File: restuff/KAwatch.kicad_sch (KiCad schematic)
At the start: 15 parts, among them J1 Conn_01x08, J2 USB_C_Receptacle_PowerOnly_6P, J3 Conn_01x02, J4 Conn_01x02, Q1 Q_NPN_BCE, SW1 SW_Push, U1 ESP32-WROOM-32E, U2 MCP73831-2-OT, U3 AMS1117-3.3

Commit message: testing bullshi
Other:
- note added: "Nig"
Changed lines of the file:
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@@
+		)
+	)
+	(text "Nig"
+		(exclude_from_sim no)
+		(at 209.804 127.508 0)
+		(effects
+			(font
+				(size 1.27 1.27)
+			)
 		)
 	)

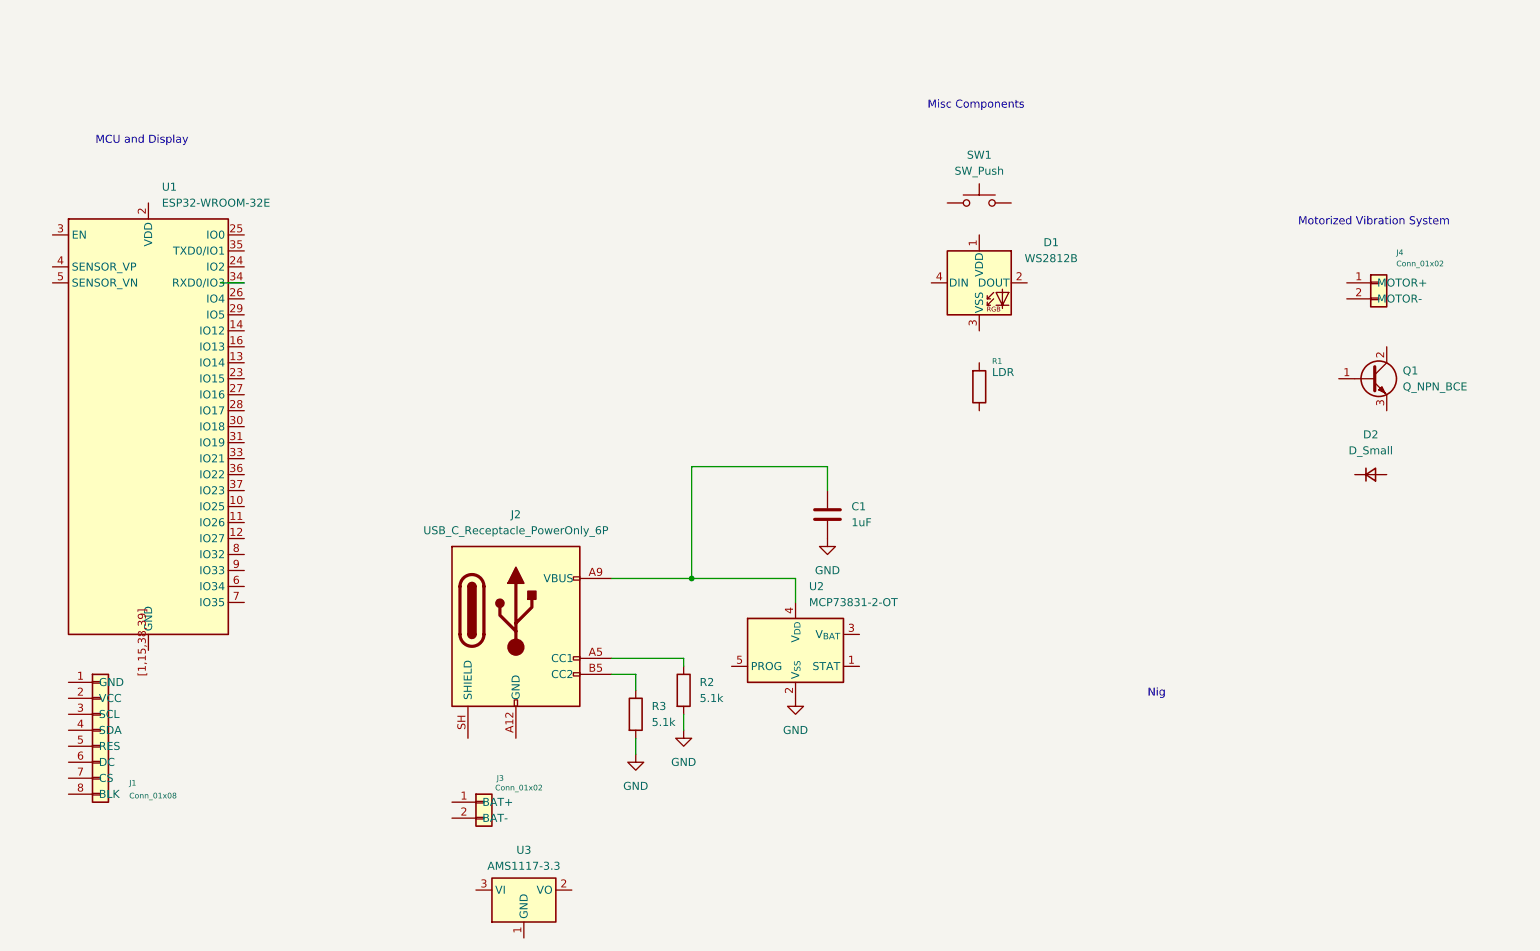
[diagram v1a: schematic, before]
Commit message: added more wires to powerchain
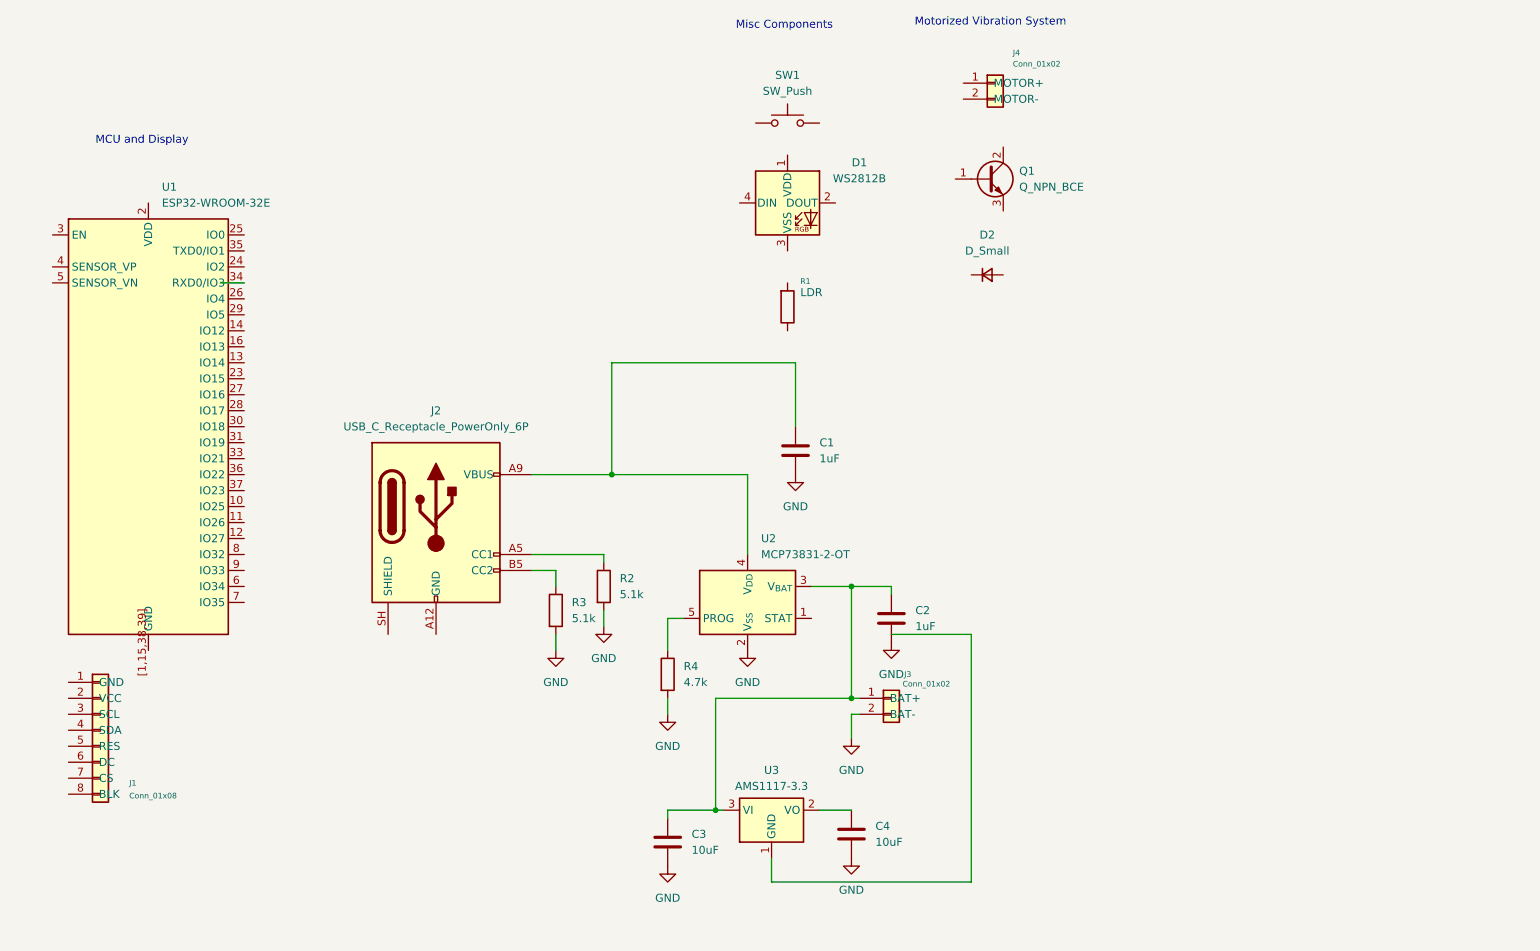
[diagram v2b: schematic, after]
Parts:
- added C2: 1uF, symbol Device:C
- added C3, C4: 10uF, symbol Device:C
- added R4: 4.7k, symbol Device:R
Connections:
- net GND: now also J3.2 (BAT-), C2.2, C3.2, C4.2, R4.2
- net at U2.3 (V_{BAT}): now also J3.1 (BAT+), U3.3 (VI), C2.1, C3.1
- net at U2.5 (PROG): now also R4.1
- net at U3.2 (VO): now also C4.1
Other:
- note removed: "Nig"
- moved on the sheet: C1, D1, D2, J2, J3, J4, Q1, R1, R2, R3, SW1, U2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

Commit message: connections to display
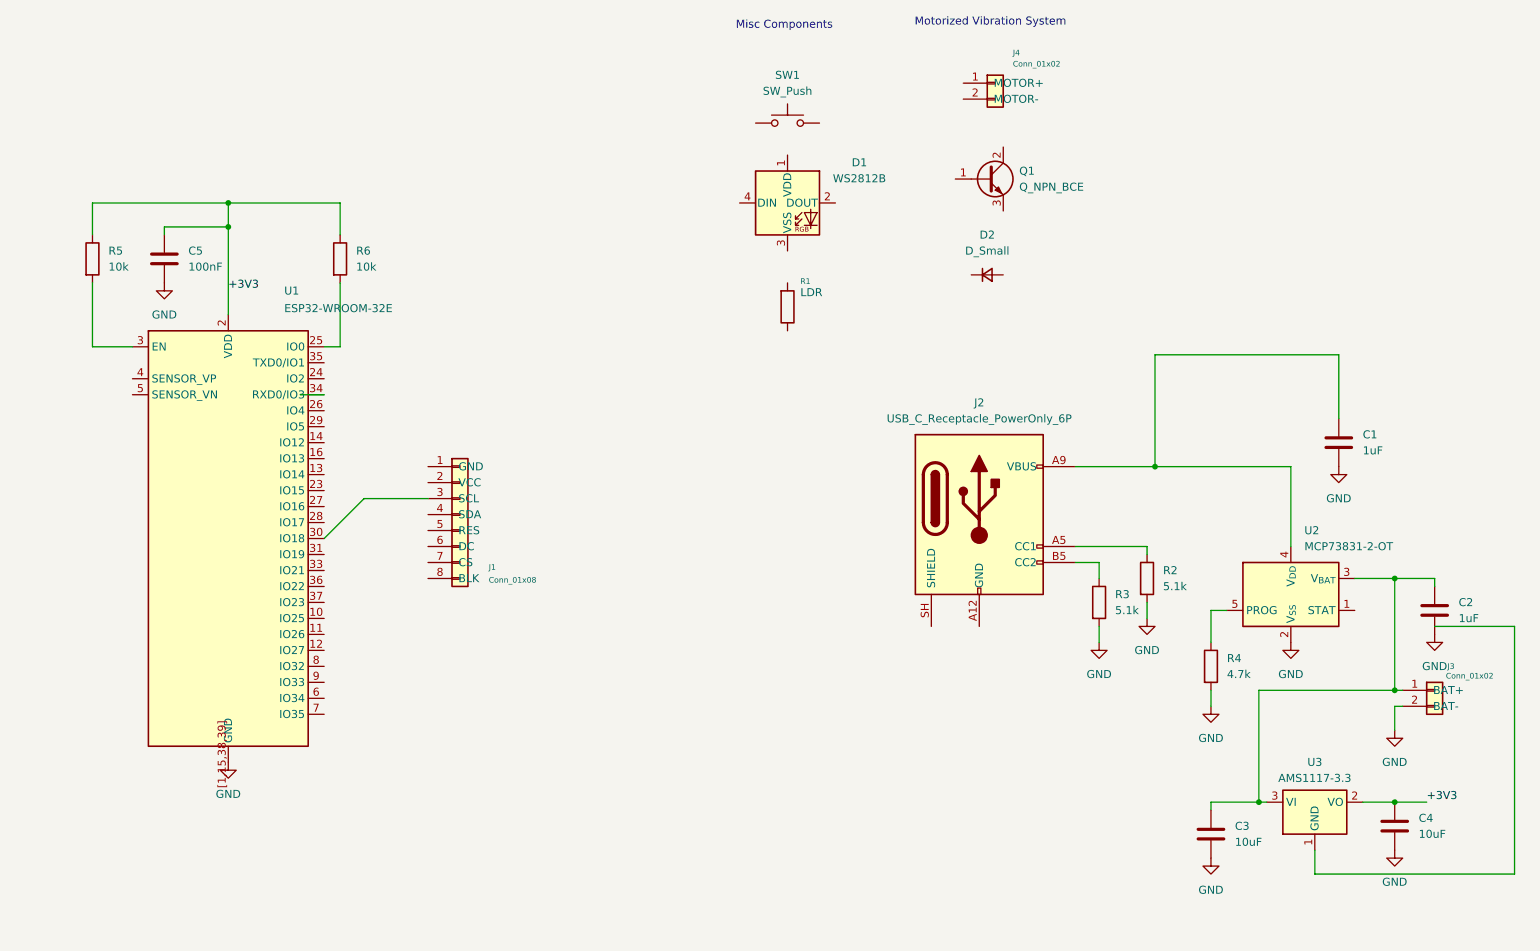
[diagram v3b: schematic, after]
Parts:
- added C5: 100nF, symbol Device:C
- added R5, R6: 10k, symbol Device:R
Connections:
- net GND: now also U1.[1,15,38,39] (GND), C5.2
- net at J1.3 (SCL): now also U1.30 (IO18)
- net +3V3: now reaches C4.1, U3.2 (VO)
- net +3V3: now also U1.2 (VDD), C5.1, R5.1, R6.1
- net at U1.25 (IO0): now also R6.2
- net at U1.3 (EN): now also R5.2
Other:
- note removed: "MCU and Display"
- moved on the sheet: C1, C2, C3, C4, J1, J2, J3, R2, R3, R4, U1, U2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

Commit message: display connector done
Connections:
- net at J1.3 (SCL), U1.30 (IO18): no longer names the net of J1.3 (SCL), U1.30 (IO18)
- net DISP_MOSI: now reaches J1.4 (SDA)
- net DISP_MOSI: now also U1.37 (IO23)
- net DISP_RST: now reaches J1.5 (RES)
- net DISP_RST: now also U1.11 (IO26)
- net DISP_DC: now reaches J1.6 (DC)
- net DISP_DC: now also U1.12 (IO27)
- net DISP_CS: now reaches J1.7 (CS)
- net DISP_CS: now also U1.29 (IO5)
- net DISP_BLK: now reaches J1.8 (BLK)
- net DISP_BLK: now also U1.10 (IO25)
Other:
- moved on the sheet: J1
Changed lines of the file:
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@@
-	(wire
-		(pts
-			(xy 93.98 96.52) (xy 83.82 96.52)
-		)
-		(stroke
-			(width 0)
-			(type default)
-		)
-	)
 	(wire
 		(pts
@@
 	(wire
 		(pts
+			(xy 77.47 118.11) (xy 80.01 118.11)
+		)
+		(stroke
+			(width 0)
+			(type default)
+		)
+	)
+	(wire
+		(pts
 			(xy 247.65 109.22) (xy 247.65 127)
 		)
@@
 	(wire
 		(pts
+			(xy 77.47 97.79) (xy 80.01 97.79)
+		)
+		(stroke
+			(width 0)
+			(type default)
+		)
+	)
+	(wire
+		(pts
 			(xy 40.64 49.53) (xy 40.64 54.61)
 		)
@@
 	(wire
 		(pts
-			(xy 83.82 96.52) (xy 77.47 102.87)
-		)
-		(stroke
-			(width 0)
-			(type default)
-		)
-	)
-	(wire
-		(pts
 			(xy 196.85 106.68) (xy 200.66 106.68)
 		)
@@
 	(wire
 		(pts
+			(xy 100.33 129.54) (xy 102.87 129.54)
+		)
+		(stroke
+			(width 0)
+			(type default)
+		)
+	)
+	(wire
+		(pts
+			(xy 100.33 124.46) (xy 102.87 124.46)
+		)
+		(stroke
+			(width 0)
+			(type default)
+		)
+	)
+	(wire
+		(pts
 			(xy 40.64 49.53) (xy 62.23 49.53)
 		)
@@
 	(wire
 		(pts
+			(xy 100.33 132.08) (xy 102.87 132.08)
+		)
+		(stroke
+			(width 0)
+			(type default)
+		)
+	)
+	(wire
+		(pts
 			(xy 196.85 104.14) (xy 208.28 104.14)
 		)
@@
 	(wire
 		(pts
+			(xy 77.47 120.65) (xy 80.01 120.65)
+		)
+		(stroke
+			(width 0)
+			(type default)
+		)
+	)
+	(wire
+		(pts
 			(xy 196.85 91.44) (xy 209.55 91.44)
 		)
@@
 	(wire
 		(pts
+			(xy 77.47 113.03) (xy 80.01 113.03)
+		)
+		(stroke
+			(width 0)
+			(type default)
+		)
+	)
+	(wire
+		(pts
 			(xy 234.95 156.21) (xy 266.7 156.21)
 		)
@@
 	(wire
 		(pts
+			(xy 77.47 102.87) (xy 80.01 102.87)
+		)
+		(stroke
+			(width 0)
+			(type default)
+		)
+	)
+	(wire
+		(pts
 			(xy 40.64 72.39) (xy 46.99 72.39)
 		)
@@
 	(wire
 		(pts
+			(xy 100.33 127) (xy 102.87 127)
+		)
+		(stroke
+			(width 0)
+			(type default)
+		)
+	)
+	(wire
+		(pts
+			(xy 77.47 115.57) (xy 80.01 115.57)
+		)
+		(stroke
+			(width 0)
+			(type default)
+		)
+	)
+	(wire
+		(pts
 			(xy 218.44 114.3) (xy 220.98 114.3)
 		)
@@
 	(wire
 		(pts
+			(xy 77.47 85.09) (xy 80.01 85.09)
+		)
+		(stroke
+			(width 0)
+			(type default)
+		)
+	)
+	(wire
+		(pts
 			(xy 218.44 144.78) (xy 218.44 146.05)
 		)
@@
 	(wire
 		(pts
+			(xy 100.33 134.62) (xy 102.87 134.62)
+		)
+		(stroke
+			(width 0)
+			(type default)
+		)
+	)
+	(wire
+		(pts
 			(xy 62.23 49.53) (xy 62.23 53.34)
 		)
@@
 	(wire
 		(pts
+			(xy 100.33 121.92) (xy 102.87 121.92)
+		)
+		(stroke
+			(width 0)
+			(type default)
+		)
+	)
+	(wire
+		(pts
 			(xy 266.7 116.84) (xy 266.7 156.21)
 		)
@@
 			(width 0)
 			(type default)
+		)
+	)
+	(label "DISP_SCK"
+		(at 80.01 102.87 0)
+		(effects
+			(font
+				(size 1.27 1.27)
+			)
+			(justify left bottom)
+		)
+	)
+	(label "DISP_MOSI"
+		(at 100.33 124.46 180)
+		(effects
+			(font
+				(size 1.27 1.27)
+			)
+			(justify right bottom)
+		)
+	)
+	(label "DISP_DC"
+		(at 80.01 120.65 0)
+		(effects
+			(font
+				(size 1.27 1.27)
+			)
+			(justify left bottom)
+		)
+	)
+	(label "DISP_SCK"
+		(at 100.33 121.92 180)
+		(effects
+			(font
+				(size 1.27 1.27)
+			)
+			(justify right bottom)
+		)
+	)
+	(label "DISP_CS"
+		(at 100.33 132.08 180)
+		(effects
+			(font
+				(size 1.27 1.27)
+			)
+			(justify right bottom)
 		)
 	)
@@
 		)
 	)
+	(label "DISP_DC"
+		(at 100.33 129.54 180)
+		(effects
+			(font
+				(size 1.27 1.27)
+			)
+			(justify right bottom)
+		)
+	)
+	(label "DISP_RST"
+		(at 80.01 118.11 0)
+		(effects
+			(font
+				(size 1.27 1.27)
+			)
+			(justify left bottom)
+		)
+	)
+	(label "DISP_BLK"
+		(at 80.01 115.57 0)
+		(effects
+			(font
+				(size 1.27 1.27)
+			)
+			(justify left bottom)
+		)
+	)
 	(label "+3V3"
 		(at 252.73 144.78 0)
@@
 			)
 			(justify left bottom)
+		)
+	)
+	(label "DISP_MOSI"
+		(at 80.01 113.03 0)
+		(effects
+			(font
+				(size 1.27 1.27)
+			)
+			(justify left bottom)
+		)
+	)
+	(label ""
+		(at 100.33 121.92 180)
+		(effects
+			(font
+				(size 1.27 1.27)
+			)
+			(justify right bottom)
+		)
+	)
+	(label "DISP_BLK"
+		(at 100.33 134.62 180)
+		(effects
+			(font
+				(size 1.27 1.27)
+			)
+			(justify right bottom)
+		)
+	)
+	(label "DISP_CS"
+		(at 80.01 85.09 0)
+		(effects
+			(font
+				(size 1.27 1.27)
+			)
+			(justify left bottom)
+		)
+	)
+	(label "DISP_RST"
+		(at 100.33 127 180)
+		(effects
+			(font
+				(size 1.27 1.27)
+			)
+			(justify right bottom)
 		)
 	)
@@
 	(symbol
 		(lib_id "Connector_Generic:Conn_01x08")
-		(at 99.06 99.06 0)
+		(at 107.95 124.46 0)
 		(unit 1)
 		(body_style 1)
@@
 		(dnp no)
 		(property "Reference" "J1"
-			(at 103.632 107.442 0)
+			(at 112.522 132.842 0)
 			(show_name no)
 			(do_not_autoplace no)
@@
 		)
 		(property "Value" "Conn_01x08"
-			(at 103.632 109.474 0)
+			(at 112.522 134.874 0)
 			(show_name no)
 			(do_not_autoplace no)
@@
 		)
 		(property "Footprint" "RF_Module:ESP32-WROOM-32E"
-			(at 99.06 99.06 0)
+			(at 107.95 124.46 0)
 			(hide yes)
 			(show_name no)
@@
 		)
 		(property "Datasheet" ""
-			(at 99.06 99.06 0)
+			(at 107.95 124.46 0)
 			(hide yes)
 			(show_name no)
@@
 		)
 		(property "Description" "Generic connector, single row, 01x08, script generated (kicad-library-utils/schlib/autogen/connector/)"
-			(at 99.06 99.06 0)
-			(hide yes)
-			(show_name no)
+			(at 107.95 124.46 0)
+			(hide yes)
+			(show_name no)

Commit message: push button wired
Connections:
- net GND: now also SW1.2
- net at SW1.1: now also U1.16 (IO13)
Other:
- moved on the sheet: J1, SW1
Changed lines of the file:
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@@
+	(wire
+		(pts
+			(xy 110.49 90.17) (xy 110.49 95.25)
+		)
+		(stroke
+			(width 0)
+			(type default)
+		)
+	)
 	(wire
 		(pts
@@
 	(wire
 		(pts
-			(xy 100.33 129.54) (xy 102.87 129.54)
-		)
-		(stroke
-			(width 0)
-			(type default)
-		)
-	)
-	(wire
-		(pts
-			(xy 100.33 124.46) (xy 102.87 124.46)
+			(xy 101.6 129.54) (xy 104.14 129.54)
+		)
+		(stroke
+			(width 0)
+			(type default)
+		)
+	)
+	(wire
+		(pts
+			(xy 101.6 124.46) (xy 104.14 124.46)
 		)
 		(stroke
@@
 	(wire
 		(pts
-			(xy 100.33 132.08) (xy 102.87 132.08)
+			(xy 101.6 132.08) (xy 104.14 132.08)
 		)
 		(stroke
@@
 	(wire
 		(pts
+			(xy 77.47 90.17) (xy 100.33 90.17)
+		)
+		(stroke
+			(width 0)
+			(type default)
+		)
+	)
+	(wire
+		(pts
 			(xy 80.01 62.23) (xy 80.01 72.39)
 		)
@@
 	(wire
 		(pts
-			(xy 100.33 127) (xy 102.87 127)
+			(xy 101.6 127) (xy 104.14 127)
 		)
 		(stroke
@@
 	(wire
 		(pts
-			(xy 100.33 134.62) (xy 102.87 134.62)
+			(xy 101.6 134.62) (xy 104.14 134.62)
 		)
 		(stroke
@@
 	(wire
 		(pts
-			(xy 100.33 121.92) (xy 102.87 121.92)
+			(xy 101.6 121.92) (xy 104.14 121.92)
 		)
 		(stroke
@@
 	)
 	(label "DISP_MOSI"
-		(at 100.33 124.46 180)
+		(at 101.6 124.46 180)
 		(effects
 			(font
@@
 	)
 	(label "DISP_SCK"
-		(at 100.33 121.92 180)
+		(at 101.6 121.92 180)
 		(effects
 			(font
@@
 	)
 	(label "DISP_CS"
-		(at 100.33 132.08 180)
+		(at 101.6 132.08 180)
 		(effects
 			(font
@@
 	)
 	(label "DISP_DC"
-		(at 100.33 129.54 180)
+		(at 101.6 129.54 180)
 		(effects
 			(font
@@
 	)
 	(label ""
-		(at 100.33 121.92 180)
+		(at 101.6 121.92 180)
 		(effects
 			(font
@@
 	)
 	(label "DISP_BLK"
-		(at 100.33 134.62 180)
+		(at 101.6 134.62 180)
 		(effects
 			(font
@@
 	)
 	(label "DISP_RST"
-		(at 100.33 127 180)
+		(at 101.6 127 180)
 		(effects
 			(font
@@
 	)
 	(symbol
+		(lib_id "power:GND")
+		(at 110.49 95.25 0)
+		(unit 1)
+		(body_style 1)
+		(exclude_from_sim no)
+		(in_bom yes)
+		(on_board yes)
+		(in_pos_files yes)
+		(dnp no)
+		(fields_autoplaced yes)
+		(property "Reference" "#PWR012"
+			(at 110.49 101.6 0)
+			(hide yes)
+			(show_name no)
+			(do_not_autoplace no)
+			(effects
+				(font
+					(size 1.27 1.27)
+				)
+			)
+		)
+		(property "Value" "GND"
+			(at 110.49 100.33 0)
+			(show_name no)
+			(do_not_autoplace no)
+			(effects
+				(font
+					(size 1.27 1.27)
+				)
+			)
+		)
+		(property "Footprint" ""
+			(at 110.49 95.25 0)
+			(hide yes)
+			(show_name no)
+			(do_not_autoplace no)
+			(effects
+				(font
+					(size 1.27 1.27)
+				)
+			)
+		)
+		(property "Datasheet" ""
+			(at 110.49 95.25 0)
+			(hide yes)
+			(show_name no)
+			(do_not_autoplace no)
+			(effects
+				(font
+					(size 1.27 1.27)
+				)
+			)
+		)
+		(property "Description" "Power symbol creates a global label with name \"GND\" , ground"
+			(at 110.49 95.25 0)
+			(hide yes)
+			(show_name no)
+			(do_not_autoplace no)
+			(effects
+				(font
+					(size 1.27 1.27)
+				)
+			)
+		)
+		(pin "1"
+		)
+		(instances
+			(project "KAwatch"
+				(path "/d13b4dc6-0a30-4e9b-a54d-0e2e2d77415c"
+					(reference "#PWR012")
+					(unit 1)
+				)
+			)
+		)
+	)
+	(symbol
 		(lib_id "Switch:SW_Push")
-		(at 151.13 36.83 0)
+		(at 105.41 90.17 0)
 		(unit 1)
 		(body_style 1)
@@
 		(fields_autoplaced yes)
 		(property "Reference" "SW1"
-			(at 151.13 29.21 0)
+			(at 105.41 82.55 0)
 			(show_name no)
 			(do_not_autoplace no)
@@
 		)
 		(property "Value" "SW_Push"
-			(at 151.13 31.75 0)
+			(at 105.41 85.09 0)
 			(show_name no)
 			(do_not_autoplace no)
@@
 		)
 		(property "Footprint" ""
-			(at 151.13 31.75 0)
+			(at 105.41 85.09 0)
 			(hide yes)
 			(show_name no)
@@
 		)
 		(property "Datasheet" ""
-			(at 151.13 31.75 0)
+			(at 105.41 85.09 0)
 			(hide yes)
 			(show_name no)
@@
 		)
 		(property "Description" "Push button switch, generic, two pins"
-			(at 151.13 36.83 0)
+			(at 105.41 90.17 0)
 			(hide yes)
 			(show_name no)
@@
 	(symbol
 		(lib_id "Connector_Generic:Conn_01x08")
-		(at 107.95 124.46 0)
+		(at 109.22 124.46 0)
 		(unit 1)
 		(body_style 1)
@@
 		(dnp no)
 		(property "Reference" "J1"
-			(at 112.522 132.842 0)
+			(at 113.792 132.842 0)
 			(show_name no)
 			(do_not_autoplace no)
@@
 		)
 		(property "Value" "Conn_01x08"
-			(at 112.522 134.874 0)
+			(at 113.792 134.874 0)
 			(show_name no)
 			(do_not_autoplace no)
@@
 		)
 		(property "Footprint" "RF_Module:ESP32-WROOM-32E"
-			(at 107.95 124.46 0)
+			(at 109.22 124.46 0)
 			(hide yes)
 			(show_name no)
@@
 		)
 		(property "Datasheet" ""
-			(at 107.95 124.46 0)
+			(at 109.22 124.46 0)
 			(hide yes)
 			(show_name no)
@@
 		)
 		(property "Description" "Generic connector, single row, 01x08, script generated (kicad-library-utils/schlib/autogen/connector/)"
-			(at 107.95 124.46 0)
-			(hide yes)
-			(show_name no)
+			(at 109.22 124.46 0)
+			(hide yes)
+			(show_name no)

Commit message: motor components added
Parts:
- added R7: 1k, symbol Device:R
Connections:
- net +3V3: now also D1.1 (VDD), J4.1 (MOTOR+)
- net GND: now also D1.3 (VSS), Q1.3 (E)
- net at J4.2 (MOTOR-): now also Q1.2 (C)
- net at Q1.1 (B): now also R7.2
- net at D1.4 (DIN): now also U1.26 (IO4)
- net at U1.13 (IO14): now also R7.1
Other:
- moved on the sheet: C1, C2, C3, C4, D1, D2, J1, J2, J3, J4, Q1, R1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
